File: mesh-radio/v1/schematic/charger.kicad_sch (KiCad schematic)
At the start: 25 parts, among them J3 S2B-PH-SM4-TB(LF)(SN), Q1 CSD25485F5, Q2 SSM10N954L,EFF, U4 BQ25185DLHR, U5 BQ29700DSER

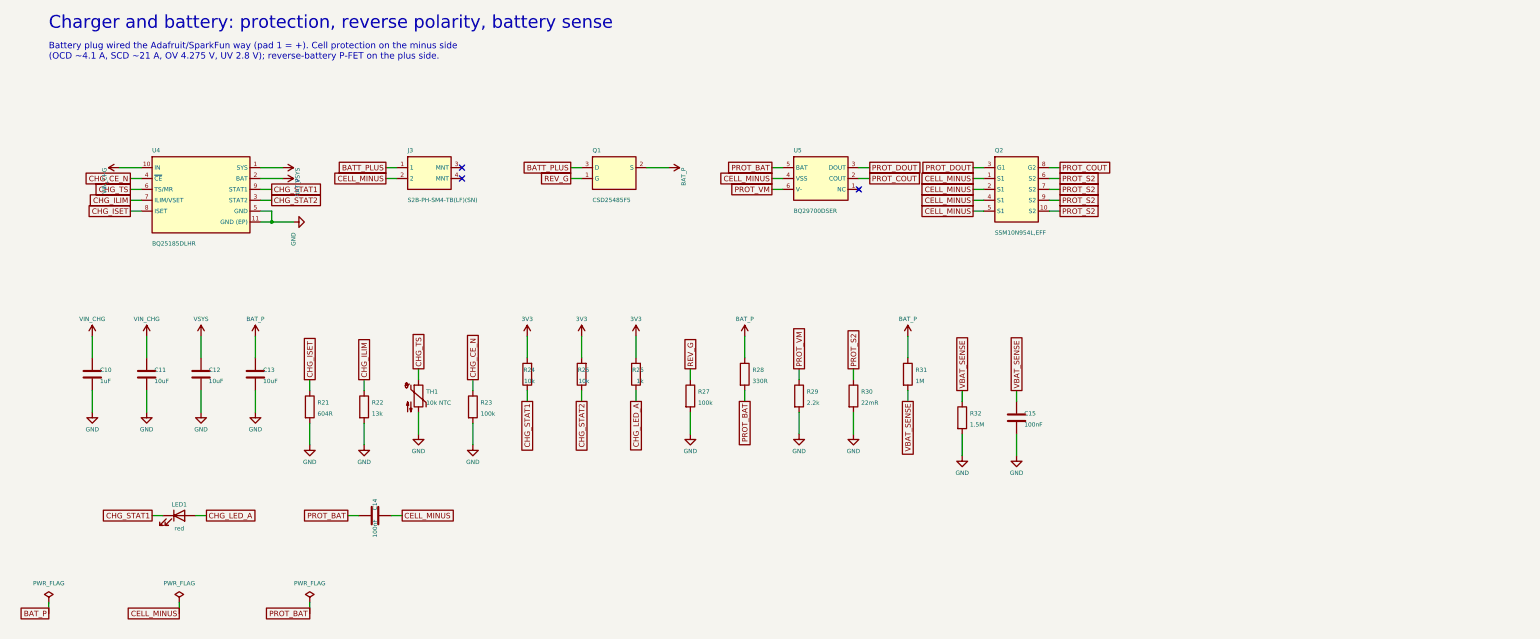
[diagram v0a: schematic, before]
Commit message: Mesh Radio v1: fix every design-review finding, add the part audit
An independent review of the schematic found two critical and nine further
issues; all are fixed in src/circuit.py:
- reverse-battery FET gate now returns to the cell's own minus terminal, so
  a backwards cell stays isolated even while USB/solar/drone power the board
- solar and drone inputs: reverse-blocking Schottky + 22 V flat-clamp TVS
  (the 15 V TVS would have failed on a 12 V panel); 4.7 V clamp on every
  eFuse EN/UVLO pin so 20 V on an input stays inside its rating
- ideal diode (LM66100) holds VSYS on the cell when a 3 W burst trips the
  charger's 3.0 V battery disconnect
- charge LED moved to STAT2 (charging), USB cut-off lowered to 5.4 V,
  charger /CE on a GPIO for firmware temperature control, -40 C TCXO,
  power mux on only with the amplifier, header VSYS pin removed
- firmware ceilings documented: SX1262 +20 dBm, amplifier 3.6 V by default

docs/part-audit.md: all 125 lines checked at DigiKey and LCSC (genuine
LCSC numbers, DigiKey numbers, second sources for out-of-stock lines);
parts cost about $76 at 10 boards, $58 at 100.

Schematic regenerated: ERC 0 violations, netlist equals circuit.py.

Co-Authored-By: Claude Opus 5.5 <noreply@anthropic.com>
Claude-Session: https://claude.ai/code/session_015TBB2ThqxHSgA8MkFosmn9
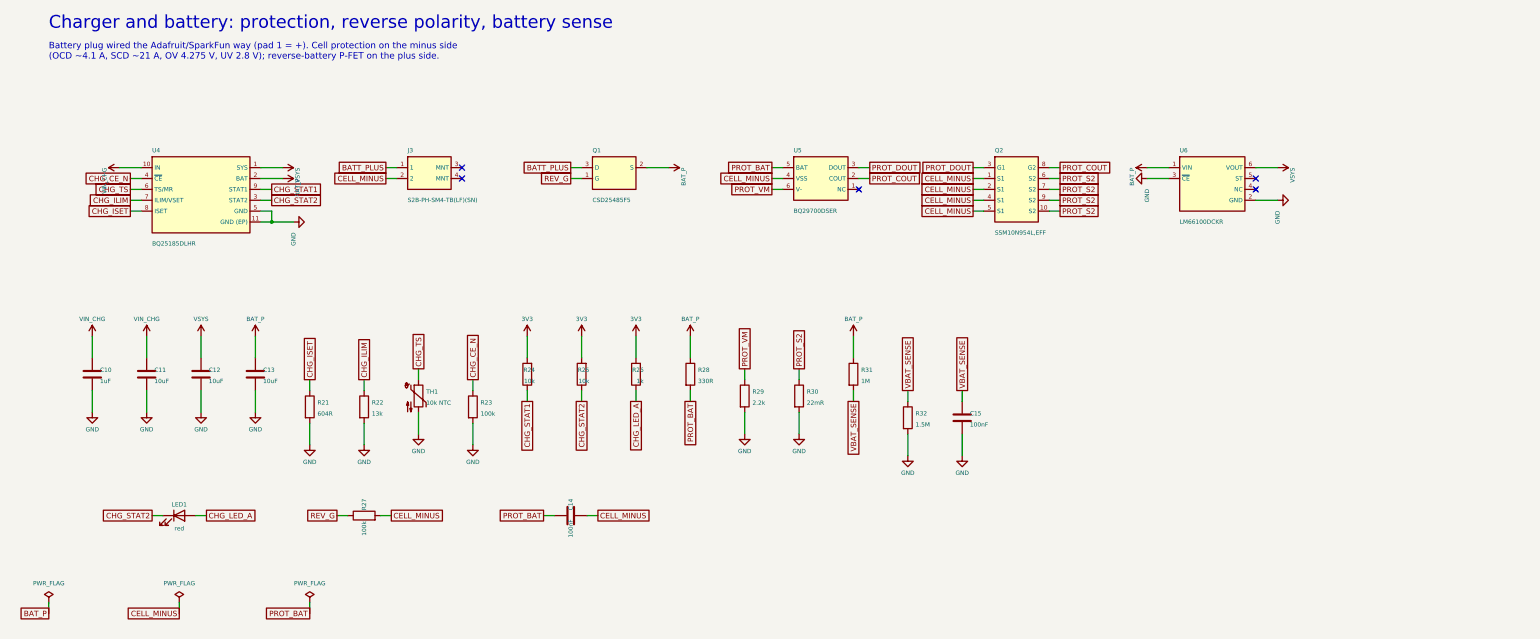
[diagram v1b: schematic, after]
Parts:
- added U6: LM66100DCKR, og:SC-70-6, symbol og:LM66100
- C10: DigiKey (none) -> 1276-1184-1-ND
- C11, C12, C13: DigiKey (none) -> 1276-2891-1-ND
- C14, C15: DigiKey (none) -> 1276-1001-1-ND
- J3: DigiKey (none) -> 455-S2B-PH-SM4-TBCT-ND
- LED1: DigiKey (none) -> 160-1447-1-ND
- Q1: DigiKey (none) -> 296-47760-1-ND
- Q2: DigiKey (none) -> 264-SSM10N954LEFFCT-ND
- R21: DigiKey (none) -> YAG3199CT-ND
- R22: DigiKey (none) -> 311-13.0KLRCT-ND
- R23, R27: DigiKey (none) -> 311-100KLRCT-ND
- R24, R25: DigiKey (none) -> 311-10.0KLRCT-ND
- R26: DigiKey (none) -> 311-1.00KLRCT-ND
- R28: DigiKey (none) -> 311-330LRCT-ND
- R29: DigiKey (none) -> 311-2.20KLRCT-ND
- R30: DigiKey (none) -> P.022AUCT-ND
- R31: DigiKey (none) -> 311-1.00MLRCT-ND
- R32: DigiKey (none) -> 13-RC0402FR-071M5LCT-ND
- TH1: DigiKey (none) -> 490-4801-1-ND
- U4: DigiKey (none) -> 296-BQ25185DLHRCT-ND
- U5: DigiKey (none) -> 296-43985-1-ND
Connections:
- net BAT_P: now also U6.1 (VIN)
- net CELL_MINUS: now also R27.2
- net CHG_STAT1: no longer LED1.1 (K)
- net CHG_STAT2: now also LED1.1 (K)
- net GND: now also U6.2 (GND), U6.3 (~{CE}); no longer R27.2
- net VSYS: now also U6.6 (VOUT)
- no-connect marks 3 -> 5
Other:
- moved on the sheet: C14, C15, R27, R28, R29, R30, R31, R32

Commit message: Mesh radio v1: power-path and firmware rework in progress (snapshot)
Co-Authored-By: Claude Opus 5.5 <noreply@anthropic.com>
Claude-Session: https://claude.ai/code/session_015TBB2ThqxHSgA8MkFosmn9
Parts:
- removed C15: 100nF, og:C_0402, symbol Device:C
- removed R21: 604R, og:R_0402, symbol Device:R
- removed R22: 13k, og:R_0402, symbol Device:R
- added C9: 1uF, og:C_0603, symbol Device:C
- added D7: RB060MM-30, og:SOD-123FL, symbol og_device:D_Schottky_RB060MM
- added Q3: SSM10N954L,EFF, og:CSP-10L_SSM10N954L, symbol og:SSM10N954L
- added R33: 2.2k, og:R_0402, symbol Device:R
- added R34: 15mR, og:R_1206, symbol Device:R
- added R35: 1.15k, og:R_0402, symbol Device:R
- added R36: 1M, og:R_0402, symbol Device:R
- added R37: 1.5M, og:R_0402, symbol Device:R
- C10: value 1uF -> 10uF; footprint og:C_0603 -> og:C_0805; DigiKey 1276-1184-1-ND -> 1276-2891-1-ND; LCSC C29936 -> C15850; MPN CL10B105KA8NNNC -> CL21A106KAYNNNE
- C12, C13: value 10uF -> 100nF; footprint og:C_0805 -> og:C_0402; DigiKey 1276-2891-1-ND -> 1276-1001-1-ND; LCSC C15850 -> C1525; MPN CL21A106KAYNNNE -> CL05B104KO5NNNC
- Q1: value CSD25485F5 -> CSD25310Q2T; footprint og:PICOSTAR-3_L1.6-W0.8-P0.53-L -> og:WSON-6_DQK_CSD25310Q2; symbol og:CSD25485F5 -> og:CSD25310Q2; DigiKey 296-47760-1-ND -> 296-50290-1-ND; LCSC C2867111 -> C2871649; MPN CSD25485F5 -> CSD25310Q2T
- Q2: value SSM10N954L,EFF -> SSM3K56ACT; footprint og:CSP-10L_SSM10N954L -> og:SOT-883; symbol og:SSM10N954L -> og_device:Q_NMOS_NMOS; DigiKey 264-SSM10N954LEFFCT-ND -> SSM3K56ACTL3FCT-ND; LCSC C5274420 -> C146308; MPN SSM10N954L,EFF -> SSM3K56ACT,L3F
- R23: value 100k -> 1k; DigiKey 311-100KLRCT-ND -> 311-1.00KLRCT-ND; LCSC C60491 -> C106235; MPN RC0402FR-07100KL -> RC0402FR-071KL
- R24: value 10k -> 13k; DigiKey 311-10.0KLRCT-ND -> 311-13.0KLRCT-ND; LCSC C60490 -> C138057; MPN RC0402FR-0710KL -> RC0402FR-0713KL
- R25: value 10k -> 100k; DigiKey 311-10.0KLRCT-ND -> 311-100KLRCT-ND; LCSC C60490 -> C60491; MPN RC0402FR-0710KL -> RC0402FR-07100KL
- R26: value 1k -> 10k; DigiKey 311-1.00KLRCT-ND -> 311-10.0KLRCT-ND; LCSC C106235 -> C60490; MPN RC0402FR-071KL -> RC0402FR-0710KL
- R27: value 100k -> 10k; DigiKey 311-100KLRCT-ND -> 311-10.0KLRCT-ND; LCSC C60491 -> C60490; MPN RC0402FR-07100KL -> RC0402FR-0710KL
- R28: value 330R -> 1k; DigiKey 311-330LRCT-ND -> 311-1.00KLRCT-ND; LCSC C105875 -> C106235; MPN RC0402FR-07330RL -> RC0402FR-071KL
- R29: value 2.2k -> 1M; DigiKey 311-2.20KLRCT-ND -> 311-1.00MLRCT-ND; LCSC C114762 -> C138033; MPN RC0402FR-072K2L -> RC0402FR-071ML
- R30: value 22mR -> 1M; footprint og:R_1206 -> og:R_0402; DigiKey P.022AUCT-ND -> 311-1.00MLRCT-ND; LCSC C2075813 -> C138033; MPN ERJ-8BWFR022V -> RC0402FR-071ML; Manufacturer Panasonic -> Yageo
- R31: value 1M -> 100k; DigiKey 311-1.00MLRCT-ND -> 311-100KLRCT-ND; LCSC C138033 -> C60491; MPN RC0402FR-071ML -> RC0402FR-07100KL
- R32: value 1.5M -> 330R; DigiKey 13-RC0402FR-071M5LCT-ND -> 311-330LRCT-ND; LCSC C138034 -> C105875; MPN RC0402FR-071M5L -> RC0402FR-07330RL
- U6: value LM66100DCKR -> TPS22950YBHR; footprint og:SC-70-6 -> og:DSBGA-6_L1.2-W0.8-R2-C3-P0.40-BL; symbol og:LM66100 -> og:TPS22950; DigiKey (none) -> 296-TPS22950YBHRCT-ND; LCSC C2869734 -> C3230039; MPN LM66100DCKR -> TPS22950YBHR
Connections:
- net 3V3: now also R27.2, R28.2; no longer R24.2, R25.2
- net BATT_PLUS: now also Q1.4 (D), Q1.8 (D (EP)), R30.1, R31.1; no longer Q1.3 (D)
- net BAT_P: now also C11.1, Q1.1 (S), Q1.5 (S), Q1.6 (S), Q1.7 (S (EP)), R29.2, R32.1, U6.B1 (VIN), R36.1; no longer C13.1, R28.1, R31.1, U6.1 (VIN)
- net CELL_MINUS: now also C12.2, C13.2, R30.2, Q3.1 (S1), Q3.2 (S1), Q3.4 (S1), Q3.5 (S1); no longer C14.2, Q2.1 (S1), Q2.4 (S1), Q2.5 (S1), R27.2
- net CHG_CE_N: now also R25.1; no longer R23.1
- net CHG_ILIM: now also R24.1
- net CHG_ISET: now also R23.1
- net CHG_LED_A: now also R28.1; no longer R26.1
- net CHG_STAT1: now also R26.1; no longer R24.1
- net CHG_STAT2: now also R27.1; no longer R25.1
- net GND: now also C14.2, R24.2, R25.2, U6.C1 (GND), C9.2, R33.2, R34.2, R35.2, R37.2; no longer C12.2, C13.2, R29.2, R30.2, R32.2, U6.2 (GND), U6.3 (~{CE})
- net PROT_BAT: now also C13.1, R32.2; no longer C14.1, R28.2
- net PROT_COUT: now also Q3.8 (G2); no longer Q2.8 (G2)
- net PROT_DOUT: now also Q3.3 (G1); no longer Q2.3 (G1)
- net PROT_S2: now also Q3.10 (S2), Q3.6 (S2), Q3.7 (S2), Q3.9 (S2), R34.1; no longer Q2.10 (S2), Q2.6 (S2), Q2.7 (S2), Q2.9 (S2), R30.1
- net PROT_VM: now also R33.1; no longer R29.1
- net REV_G: now also Q1.3 (G), Q2.3 (D), R29.1; no longer Q1.1 (G), R27.1
- net VBAT_SENSE: now also C14.1, R36.2, R37.1; no longer R31.2, R32.1
- net VIN_CHG: now also C9.1; no longer C10.1, C11.1
- net VSYS: now also C10.1, D7.1 (K); no longer C12.1, U6.6 (VOUT)
- new net BYP_ILIM: R35.1, U6.C2 (ILIM)
- new net BYP_OUT: D7.2 (A), U6.B2 (VOUT)
- new net POL_G: C12.1, Q2.1 (G), R31.2
- new net PWR_ON: U6.A1 (ON)
- no-connect marks 5 -> 4
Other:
- note added: "Battery plug wired the Adafruit/SparkFun way (pad 1 = +). Cell protection on the minus side (OCD ~5.8 A, SCD ~29 A, OV 4.275 V, UV 2.8 V); reverse-battery P-FET on the plus side, on only when the cell is the right way round. Charge 300 mA. Current-limited cell-to-SYS bypass."
- note removed: "Battery plug wired the Adafruit/SparkFun way (pad 1 = +). Cell protection on the minus side (OCD ~4.1 A, SCD ~21 A, OV 4.275 V, UV 2.8 V); reverse-battery P-FET on the plus side."
- moved on the sheet: C10, C11, C12, C13, C14, J3, LED1, R23, R24, R25, R26, R27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

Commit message: Mesh Radio v1 schematic: regenerated (gate clamp, NTC part); ERC 0, netlist equal
Co-Authored-By: Claude Opus 5.5 <noreply@anthropic.com>
Claude-Session: https://claude.ai/code/session_015TBB2ThqxHSgA8MkFosmn9
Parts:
- added D8: RB060MM-30, og:SOD-123FL, symbol og_device:D_Schottky_RB060MM
- D7: value RB060MM-30 -> 4.7V; footprint og:SOD-123FL -> og:SOD-323FL; symbol og_device:D_Schottky_RB060MM -> og_device:D_Zener_ZENER4V7; DigiKey RB060MM-30CT-ND -> (none); LCSC C308720 -> C209560; MPN RB060MM-30TR -> UDZVTE-174.7B
- TH1: DigiKey 490-4801-1-ND -> 490-18149-1-ND; LCSC C77131 -> C237326; MPN NCP15XH103F03RC -> NCU15XH103F60RC
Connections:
- net BYP_OUT: now also D8.2 (A); no longer D7.2 (A)
- net CELL_MINUS: now also D7.2 (A)
- net POL_G: now also D7.1 (K)
- net VSYS: now also D8.1 (K); no longer D7.1 (K)
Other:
- moved on the sheet: C13, D7
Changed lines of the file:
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@@
 			)
 		)
-		(property "MPN" "NCP15XH103F03RC"
+		(property "MPN" "NCU15XH103F60RC"
 			(at 88.9 104.14 0)
 			(effects
@@
 			)
 		)
-		(property "DigiKey" "490-4801-1-ND"
+		(property "DigiKey" "490-18149-1-ND"
 			(at 88.9 104.14 0)
 			(effects
@@
 			)
 		)
-		(property "LCSC" "C77131"
+		(property "LCSC" "C237326"
 			(at 88.9 104.14 0)
 			(effects
@@
 		(on_board yes)
 		(dnp no)
-		(property "Reference" "D7"
+		(property "Reference" "D8"
 			(at 217.7 98.06 0)
 			(effects
@@
 			(project "mesh-radio"
 				(path "/1e0df660-60b5-6ed0-6a2a-f5098e72ebfd/9f171647-52ea-aa63-c2e7-0af4c9c3ce05"
-					(reference "D7")
+					(reference "D8")
 					(unit 1)
 				)
@@
 	)
 	(symbol
+		(lib_id "og_device:D_Zener_ZENER4V7")
+		(at 223.52 132.08 0)
+		(unit 1)
+		(exclude_from_sim no)
+		(in_bom yes)
+		(on_board yes)
+		(dnp no)
+		(property "Reference" "D7"
+			(at 223.52 129.48 0)
+			(effects
+				(font
+					(size 1 1)
+				)
+			)
+		)
+		(property "Value" "4.7V"
+			(at 223.52 135.08 0)
+			(effects
+				(font
+					(size 1 1)
+				)
+			)
+		)
+		(property "Footprint" "og:SOD-323FL"
+			(at 223.52 132.08 0)
+			(effects
+				(font
+					(size 1.27 1.27)
+				)
+				(hide yes)
+			)
+		)
+		(property "MPN" "UDZVTE-174.7B"
+			(at 223.52 132.08 0)
+			(effects
+				(font
+					(size 1.27 1.27)
+				)
+				(hide yes)
+			)
+		)
+		(property "Manufacturer" "Rohm"
+			(at 223.52 132.08 0)
+			(effects
+				(font
+					(size 1.27 1.27)
+				)
+				(hide yes)
+			)
+		)
+		(property "LCSC" "C209560"
+			(at 223.52 132.08 0)
+			(effects
+				(font
+					(size 1.27 1.27)
+				)
+				(hide yes)
+			)
+		)
+		(property "Description" "Zener 4.7 V 200 mW, SOD-323FL"
+			(at 223.52 132.08 0)
+			(effects
+				(font
+					(size 1.27 1.27)
+				)
+				(hide yes)
+			)
+		)
+		(instances
+			(project "mesh-radio"
+				(path "/1e0df660-60b5-6ed0-6a2a-f5098e72ebfd/9f171647-52ea-aa63-c2e7-0af4c9c3ce05"
+					(reference "D7")
+					(unit 1)
+				)
+			)
+		)
+	)
+	(wire
+		(pts
+			(xy 219.71 132.08)
+			(xy 217.17 132.08)
+		)
+		(stroke
+			(width 0)
+			(type default)
+		)
+	)
+	(global_label "POL_G"
+		(shape passive)
+		(at 217.17 132.08 180)
+		(fields_autoplaced yes)
+		(effects
+			(font
+				(size 1.27 1.27)
+			)
+			(justify right)
+		)
+		(property "Intersheetrefs" "${INTERSHEET_REFS}"
+			(at 217.17 132.08 0)
+			(effects
+				(font
+					(size 1.27 1.27)
+				)
+				(justify right)
+				(hide yes)
+			)
+		)
+	)
+	(wire
+		(pts
+			(xy 227.33 132.08)
+			(xy 229.87 132.08)
+		)
+		(stroke
+			(width 0)
+			(type default)
+		)
+	)
+	(global_label "CELL_MINUS"
+		(shape passive)
+		(at 229.87 132.08 0)
+		(fields_autoplaced yes)
+		(effects
+			(font
+				(size 1.27 1.27)
+			)
+			(justify left)
+		)
+		(property "Intersheetrefs" "${INTERSHEET_REFS}"
+			(at 229.87 132.08 0)
+			(effects
+				(font
+					(size 1.27 1.27)
+				)
+				(justify left)
+				(hide yes)
+			)
+		)
+	)
+	(symbol
 		(lib_id "Device:C")
-		(at 226.06 132.08 90)
+		(at 271.78 132.08 90)
 		(unit 1)
 		(exclude_from_sim no)
@@
 		(dnp no)
 		(property "Reference" "C13"
-			(at 226.06 129.48 0)
+			(at 271.78 129.48 0)
 			(effects
 				(font
@@
 		)
 		(property "Value" "100nF"
-			(at 226.06 135.08 0)
+			(at 271.78 135.08 0)
 			(effects
 				(font
@@
 		)
 		(property "Footprint" "og:C_0402"
-			(at 226.06 132.08 0)
+			(at 271.78 132.08 0)
 			(effects
 				(font
@@
 		)
 		(property "MPN" "CL05B104KO5NNNC"
-			(at 226.06 132.08 0)
+			(at 271.78 132.08 0)
 			(effects
 				(font
@@
 		)
 		(property "Manufacturer" "Samsung Electro-Mechanics"
-			(at 226.06 132.08 0)
+			(at 271.78 132.08 0)
 			(effects
 				(font
@@
 		)
 		(property "DigiKey" "1276-1001-1-ND"
-			(at 226.06 132.08 0)
+			(at 271.78 132.08 0)
 			(effects
 				(font
@@
 		)
 		(property "LCSC" "C1525"
-			(at 226.06 132.08 0)
+			(at 271.78 132.08 0)
 			(effects
 				(font
@@
 		)
 		(property "Description" "Capacitor 100nF 16V X7R 0402"
-			(at 226.06 132.08 0)
+			(at 271.78 132.08 0)
 			(effects
 				(font
@@
 	(wire
 		(pts
-			(xy 222.25 132.08)
-			(xy 219.71 132.08)
+			(xy 267.97 132.08)
+			(xy 265.43 132.08)
 		)
 		(stroke
@@
 	(global_label "PROT_BAT"
 		(shape passive)
-		(at 219.71 132.08 180)
+		(at 265.43 132.08 180)
 		(fields_autoplaced yes)
 		(effects
@@
 		)
 		(property "Intersheetrefs" "${INTERSHEET_REFS}"
-			(at 219.71 132.08 0)
+			(at 265.43 132.08 0)
 			(effects
 				(font
@@
 	(wire
 		(pts
-			(xy 229.87 132.08)
-			(xy 232.41 132.08)
+			(xy 275.59 132.08)
+			(xy 278.13 132.08)
 		)
 		(stroke
@@
 	(global_label "CELL_MINUS"
 		(shape passive)
-		(at 232.41 132.08 0)
+		(at 278.13 132.08 0)
 		(fields_autoplaced yes)
 		(effects
@@
 		)
 		(property "Intersheetrefs" "${INTERSHEET_REFS}"
-			(at 232.41 132.08 0)
+			(at 278.13 132.08 0)
 			(effects
 				(font
